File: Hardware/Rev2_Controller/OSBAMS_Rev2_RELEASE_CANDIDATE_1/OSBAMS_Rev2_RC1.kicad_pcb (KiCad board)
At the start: 4 copper layers, 100 x 90 mm, 148 parts, among them J1 12V_IN, J2 ESTOP, J3 ARM, J4 K1_COIL, J5 SHUNT_KELVIN, J6 PACK_SENSE, J7 TEMP_PROBE, J8 USB-C HOST, J9 SWD, Q1 IRLML0060, SW1 RESET, U1 STM32L476RGT6, U10 USBLC6-2SC6, U2 INA228, U3 LMR14006Y, U4 VO610A-1, U5 VO610A-1, U6 CP2102N, U7 ISO7721, U9 USBLC6-2SC6

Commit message: RC1.2: CP2102N VBUS divider margin (R38 19.1k), protection marked not fully closed, isolation-rule activity check
- R38 22.1k -> 19.1k from the CP2102N datasheet limits (VIH = VDD-0.6 V; +0.12 V at VBUS 4.40 V / VDD 3.6 V / 1 %); value change only, layout unchanged
- pack-sense protection: model PASS but not closed (ERJ-P08F pulse rating, 1.5SMBJ48A leakage unread); surge-capability numbers labelled model results
- ISOLATION_RULE_CHECK: the .kicad_dru is applied from a fresh folder; pack-net rule documented as a low-voltage sense-net rule
- connector drawings still not available: footprints unchanged, item open
- ERC 0, DRC 0, unconnected 0, netlist 0 mismatches, polarity none; no Gerbers in the package

Co-Authored-By: Claude Sonnet 5.5 <noreply@anthropic.com>
Claude-Session: https://claude.ai/code/session_01HV1TCrYnLTcNjmYdFqCPLo
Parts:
- R38: value 22.1k -> 19.1k
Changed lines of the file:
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@@
 			)
 		)
-		(property "Value" "22.1k"
+		(property "Value" "19.1k"
 			(at 0 1.43 0)
 			(layer "F.Fab")
@@
 			)
 		)
-		(property "Description" "22.1k 1 % thick film 0603"
+		(property "Description" "19.1k 1 % thick film 0603"
 			(at 0 0 0)
 			(layer "F.Fab")
@@
 			)
 		)
-		(property "MPN" "CRCW060322K1FKEA"
+		(property "MPN" "CRCW060319K1FKEA"
 			(at 0 0 0)
 			(layer "F.Fab")

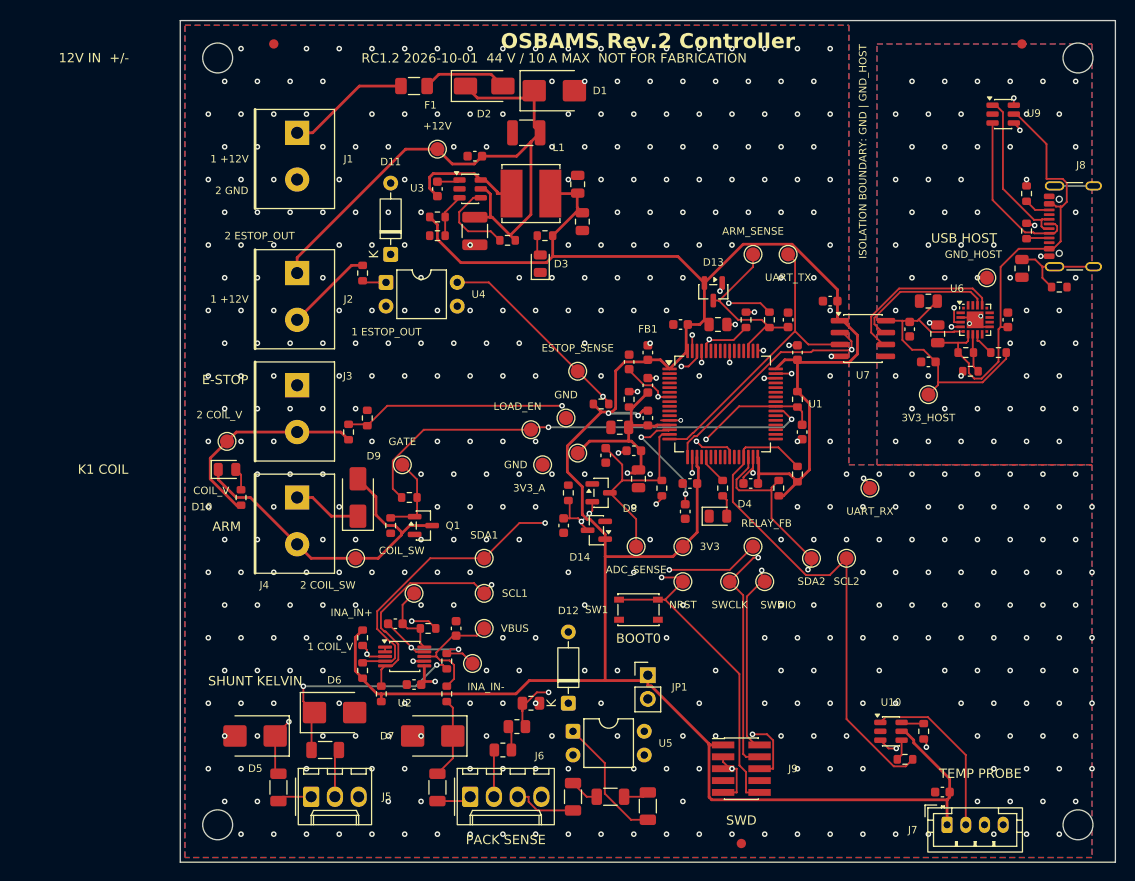
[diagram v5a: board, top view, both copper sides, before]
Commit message: RC1.2c: connector drawings checked (JST, GCT verified; J8 moved 0.275 mm), Bourns TVS data verified, Molex product facts
- GCT USB4105: footprint matches the drawing; connector was 0.275 mm too close to the board edge -> J8 x 96.600 -> 96.325, board re-routed
- JST B4B-PH-K-S footprint verified (pitch, hole, outline, pin 1, mating); Molex KK-254: product pages only, sales drawings still needed; Samtec: spec sheet has no print
- Bourns 1.5SMBJ48A: clamp points, IR <= 1.0 uA @48 V/25 C, VBR tempco read locally; leakage vs temperature unspecified; clamp margin vs temperature added
- Panasonic file supplied is ERJP6W 0805 (NRND), not ERJ-P08F: resistor pulse rating still open; protection stays 'not fully closed'
- ERC 0, DRC 0, unconnected 0, netlist 0 mismatches (403 pads), polarity none, isolation >= 1.0 mm; no Gerbers

Co-Authored-By: Claude Sonnet 5.5 <noreply@anthropic.com>
Claude-Session: https://claude.ai/code/session_01HV1TCrYnLTcNjmYdFqCPLo
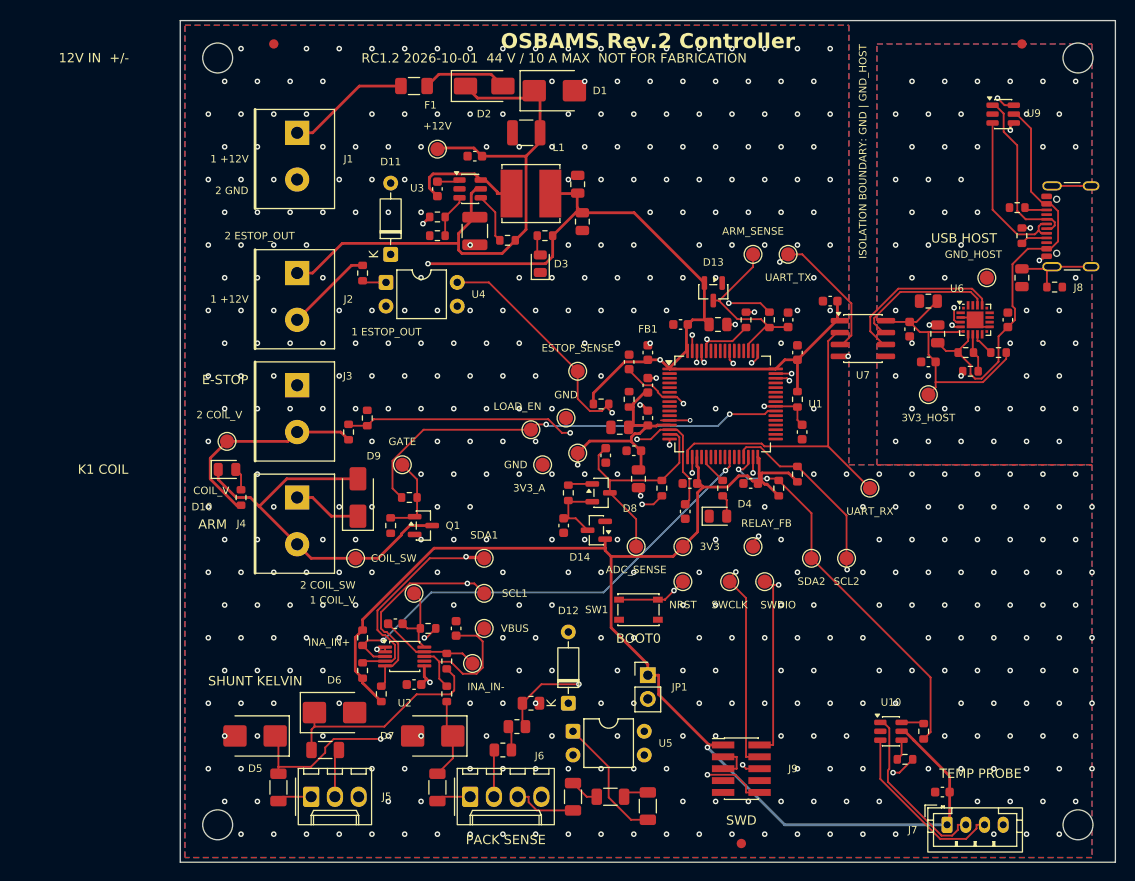
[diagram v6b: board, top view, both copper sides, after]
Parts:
- moved R9 1.80 mm to (189.5, 80.0), turned to 180 degrees
- moved C19 1.00 mm to (190.0, 87.5)
- moved R8 0.71 mm to (190.0, 83.0)
- moved R10 0.50 mm to (193.5, 88.5)
- moved J8 0.28 mm to (196.3, 82.0)
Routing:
- net INA_ALERT: track 60.2 -> 51.1 mm
- net SCL2: track 55.6 -> 47.2 mm, vias 0 -> 2
- net UART_TX_MCU: track 32.1 -> 40.3 mm, vias 0 -> 2
- net UART_RX_MCU: track 41.4 -> 35.4 mm, vias 2 -> 0
- net INA_VBUS: track 12.8 -> 17.2 mm
- net GND: track 26.9 -> 22.6 mm, vias 408 -> 418
- net SHUNT_INP_RAW: track 26.8 -> 31.1 mm
- net VBUS_USB: track 49.3 -> 45.1 mm
- net INA_INN: track 15.0 -> 10.8 mm, vias 2 -> 0
- net BUCK_EN: track 9.19 -> 5.39 mm
- net SCL2_J: track 15.1 -> 18.8 mm, vias 1 -> 0
- net COIL_SW: track 37.3 -> 40.7 mm
- net LOAD_EN: track 50.9 -> 47.7 mm
- net SDA2: track 44.7 -> 41.5 mm
- net NRST: track 61.2 -> 63.5 mm, vias 2 -> 3
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
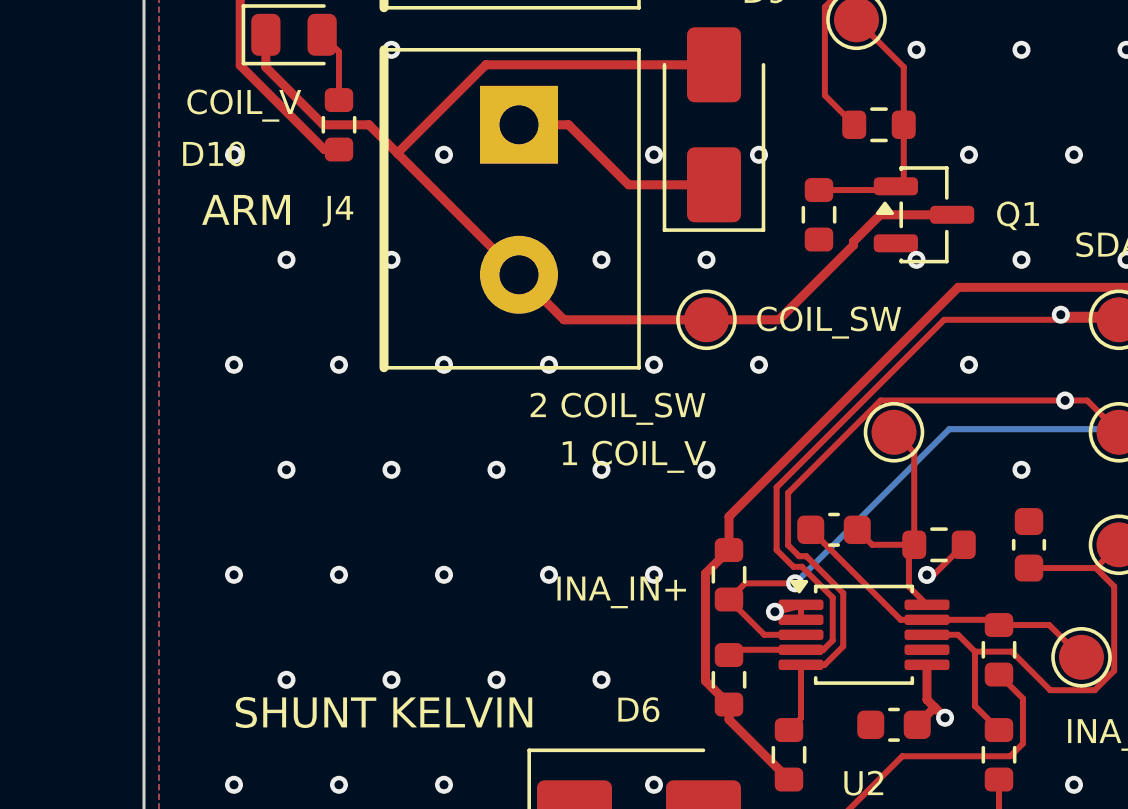
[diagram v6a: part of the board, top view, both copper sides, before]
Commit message: RC1.2d: Panasonic ERJ-P08 catalog and Samtec FTSH catalog page recorded; Molex pages repeated (no drawing)
- ERJ-P08F47R0V / ERJ-P08F10R0V: part-number scheme, 0.66 W, 500 V limiting / 1000 V overload, ESD 3 kV/150 pF read locally; no us-ms pulse curve published
- protection: PASS for the defined transient on datasheet-verified limits; TVS leakage vs temperature and resistor thermal-pulse curve remain first-article items
- Samtec FTSH-105-01-L-DV-K part number/pitch/tail span confirmed; land pattern and key position still open; Molex sales drawings (*_sd.pdf) still needed
- no board change: ERC 0, DRC 0, unconnected 0, netlist 0 mismatches, polarity none, isolation >= 1.0 mm

Co-Authored-By: Claude Sonnet 5.5 <noreply@anthropic.com>
Claude-Session: https://claude.ai/code/session_01HV1TCrYnLTcNjmYdFqCPLo
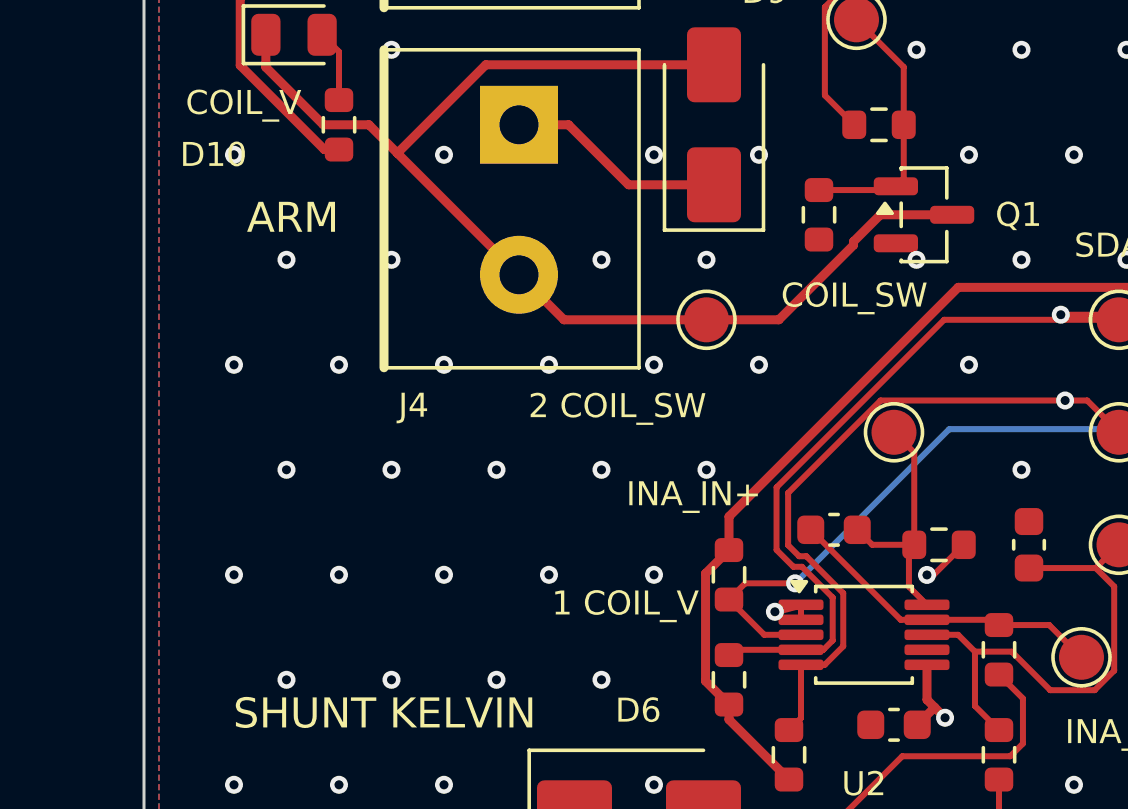
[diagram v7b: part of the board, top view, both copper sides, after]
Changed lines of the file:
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@@
 		(tags "EB21A terminal block 5.00mm")
 		(property "Reference" "J4"
-			(at -5.975001 2.8 0)
+			(at -3.5125 9.360142 0)
 			(layer "F.SilkS")
 			(effects
@@
 	)
 	(gr_text "INA_IN+"
-		(at 115.928383 126.4875 0)
+		(at 118.3225 123.310991 0)
 		(layer "F.SilkS")
 		(effects
@@
 	)
 	(gr_text "COIL_SW"
-		(at 122.825 117.5 0)
+		(at 123.6775 116.689008 0)
 		(layer "F.SilkS")
 		(effects
@@
 		)
 	)
-	(gr_text "2 COIL_SW"
-		(at 118.75 120.375 0)
+	(gr_text "1 COIL_V"
+		(at 118.49974 126.9525 0)
 		(layer "F.SilkS")
 		(effects
@@
 		)
 	)
-	(gr_text "1 COIL_V"
-		(at 118.75 121.975 0)
+	(gr_text "2 COIL_SW"
+		(at 118.75 120.375 0)
 		(layer "F.SilkS")
 		(effects
@@
 	)
 	(gr_text "ARM"
-		(at 105 113.875 0)
+		(at 106.5 114.104999 0)
 		(layer "F.SilkS")
 		(effects

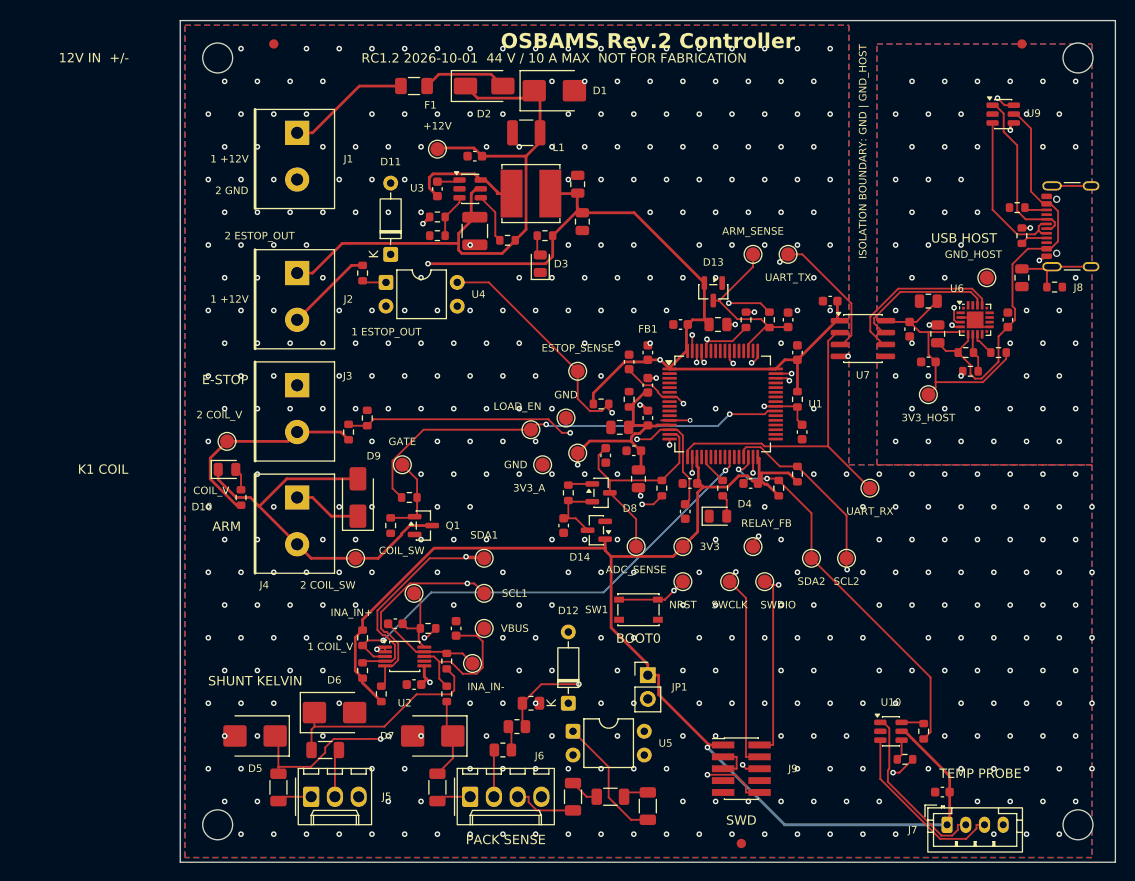
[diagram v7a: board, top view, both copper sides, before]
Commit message: RC1.2e: Samtec J9 land pattern (0.74x2.79, rev H), D15 differential clamp across INA228 IN+/IN-, protection and connector audit; ERJ-P08 pulse capability re-opened
- J9 generic footprint replaced by OSBAMS_Rev2:FTSH-105-01-L-DV-K from the Samtec recommended layout rev H; breakout re-routed
- D15 SMF12CA bidirectional TVS across INA_INP/INA_INN (INA228 differential limit +/-40 V; one Kelvin lead open)
- CONTROLLER_PROTECTION_AND_CONNECTOR_AUDIT.md (PASS / CHANGE REQUIRED / FIRST-ARTICLE VALIDATION / REMAINING FABRICATION BLOCKERS)
- rs_pulse_rating back to UNVERIFIED/critical; Molex J5/J6 stay open (3D drawing without dimensions); evidence PDFs committed
- ERC 0, DRC 0, unconnected 0, netlist 0 mismatches (405 pads), polarity OK, isolation >= 1.0 mm; 181 tests pass

Co-Authored-By: Claude Sonnet 5.5 <noreply@anthropic.com>
Claude-Session: https://claude.ai/code/session_01HV1TCrYnLTcNjmYdFqCPLo
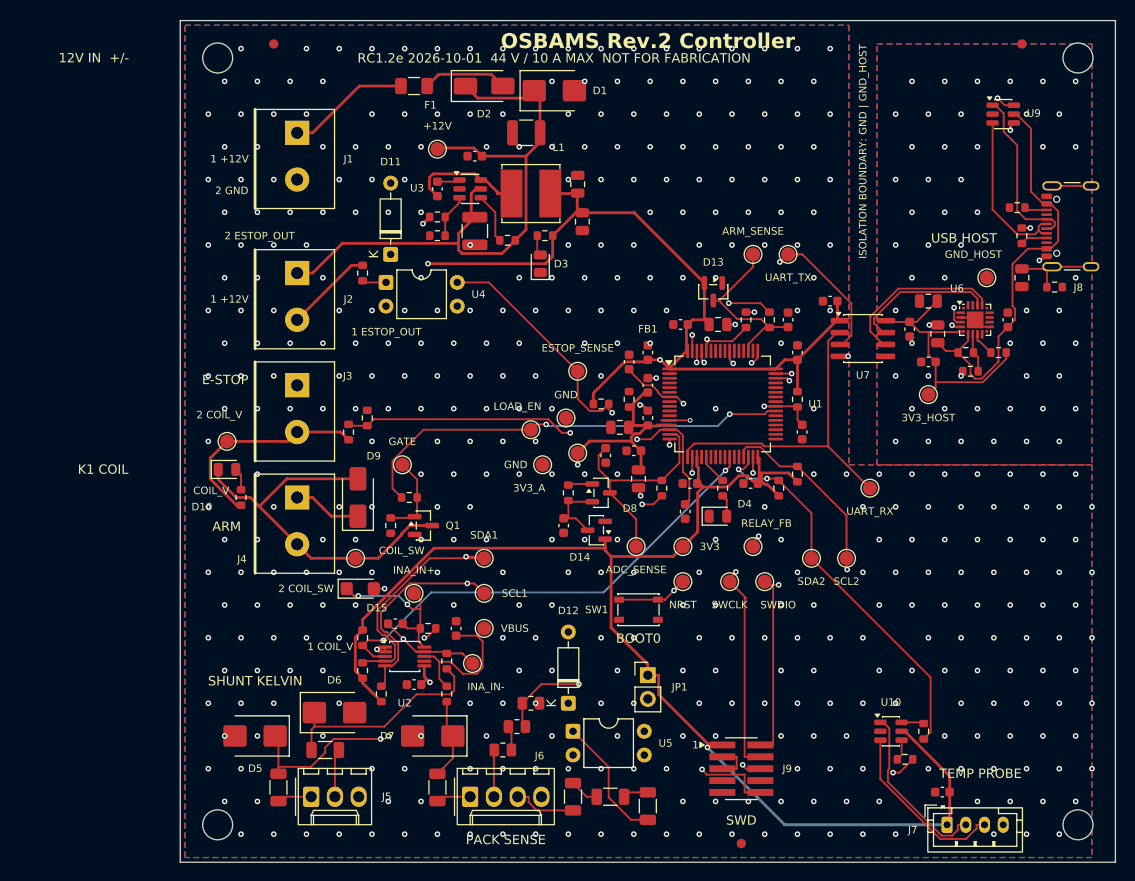
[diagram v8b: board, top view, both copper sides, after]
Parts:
- added D15: SMF12CA, Diode_SMD:D_SMF, F.Cu at (119.2, 120.8)
- J9: footprint Connector_PinHeader_1.27mm:PinHeader_2x05_P1.27mm_Vertical_SMD -> OSBAMS_Rev2:FTSH-105-01-L-DV-K
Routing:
- net INA_INP: track 8.46 -> 17.2 mm, vias 0 -> 2
- net INA_INN: track 10.8 -> 18.2 mm, vias 0 -> 2
- net NRST: track 63.5 -> 64.3 mm
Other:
- board text added: "RC1.2e 2026-10-01 44 V / 10 A MAX NOT FOR FABRICATION"
- board text removed: "RC1.2 2026-10-01 44 V / 10 A MAX NOT FOR FABRICATION"
